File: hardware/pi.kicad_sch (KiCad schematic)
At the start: 15 parts, among them J1 PI_40PIN_STACK, J10 DISP PWR 5V, J2 PI_BREAKOUT, J3 UART0 ttyAMA0, J4 UART2 ttyAMA2, J5 UART3 ttyAMA3, J6 UART4 ttyAMA4, J7 UART5 ttyAMA5, J8 I2C1 spare, J9 FAN 5V

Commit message: feat: MPN table merged into schematic fields; SES import script
Co-Authored-By: Claude Fable 5 <noreply@anthropic.com>
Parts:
- F2: MPN (none) -> Bourns MF-R200
- J1: MPN (none) -> Adafruit 1979 (2x20 stacking, extra-tall ~19.5mm) or ESQ-12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
- J10: MPN (none) -> JST B2B-XH-A(LF)(SN)
- J3, J4, J5, J6, J7, J8: MPN (none) -> JST B4B-XH-A(LF)(SN)
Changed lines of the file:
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@@
     (property "Datasheet" "" (at 69.85 95.25 0)
+      (effects (font (size 1.27 1.27)) (hide yes)))
+    (property "MPN" "Adafruit 1979 (2x20 stacking, extra-tall ~19.5mm) or ESQ-120-39-G-D" (at 69.85 95.25 0)
       (effects (font (size 1.27 1.27)) (hide yes)))
     (pin "1")
@@
     (property "Datasheet" "" (at 229.87 69.85 0)
       (effects (font (size 1.27 1.27)) (hide yes)))
+    (property "MPN" "JST B4B-XH-A(LF)(SN)" (at 229.87 69.85 0)
+      (effects (font (size 1.27 1.27)) (hide yes)))
     (pin "1")
     (pin "2")
@@
     (property "Datasheet" "" (at 260.35 69.85 0)
       (effects (font (size 1.27 1.27)) (hide yes)))
+    (property "MPN" "JST B4B-XH-A(LF)(SN)" (at 260.35 69.85 0)
+      (effects (font (size 1.27 1.27)) (hide yes)))
     (pin "1")
     (pin "2")
@@
     (property "Datasheet" "" (at 289.56 69.85 0)
       (effects (font (size 1.27 1.27)) (hide yes)))
+    (property "MPN" "JST B4B-XH-A(LF)(SN)" (at 289.56 69.85 0)
+      (effects (font (size 1.27 1.27)) (hide yes)))
     (pin "1")
     (pin "2")
@@
     (property "Datasheet" "" (at 320.04 69.85 0)
       (effects (font (size 1.27 1.27)) (hide yes)))
+    (property "MPN" "JST B4B-XH-A(LF)(SN)" (at 320.04 69.85 0)
+      (effects (font (size 1.27 1.27)) (hide yes)))
     (pin "1")
     (pin "2")
@@
     (property "Datasheet" "" (at 350.52 69.85 0)
       (effects (font (size 1.27 1.27)) (hide yes)))
+    (property "MPN" "JST B4B-XH-A(LF)(SN)" (at 350.52 69.85 0)
+      (effects (font (size 1.27 1.27)) (hide yes)))
     (pin "1")
     (pin "2")
@@
       (effects (font (size 1.27 1.27)) (hide yes)))
     (property "Datasheet" "" (at 229.87 119.38 0)
+      (effects (font (size 1.27 1.27)) (hide yes)))
+    (property "MPN" "JST B4B-XH-A(LF)(SN)" (at 229.87 119.38 0)
       (effects (font (size 1.27 1.27)) (hide yes)))
     (pin "1")
@@
     (property "Datasheet" "" (at 350.52 119.38 0)
       (effects (font (size 1.27 1.27)) (hide yes)))
+    (property "MPN" "Bourns MF-R200" (at 350.52 119.38 0)
+      (effects (font (size 1.27 1.27)) (hide yes)))
     (pin "1")
     (pin "2")
@@
     (property "Datasheet" "" (at 379.73 119.38 0)
       (effects (font (size 1.27 1.27)) (hide yes)))
-    (pin "1")
+    (property "MPN" "JST B2B-XH-A(LF)(SN)" (at 379.73 119.38 0)
+      (effects (font (size 1.27 1.27)) (hide yes)))
+    (pin "1")

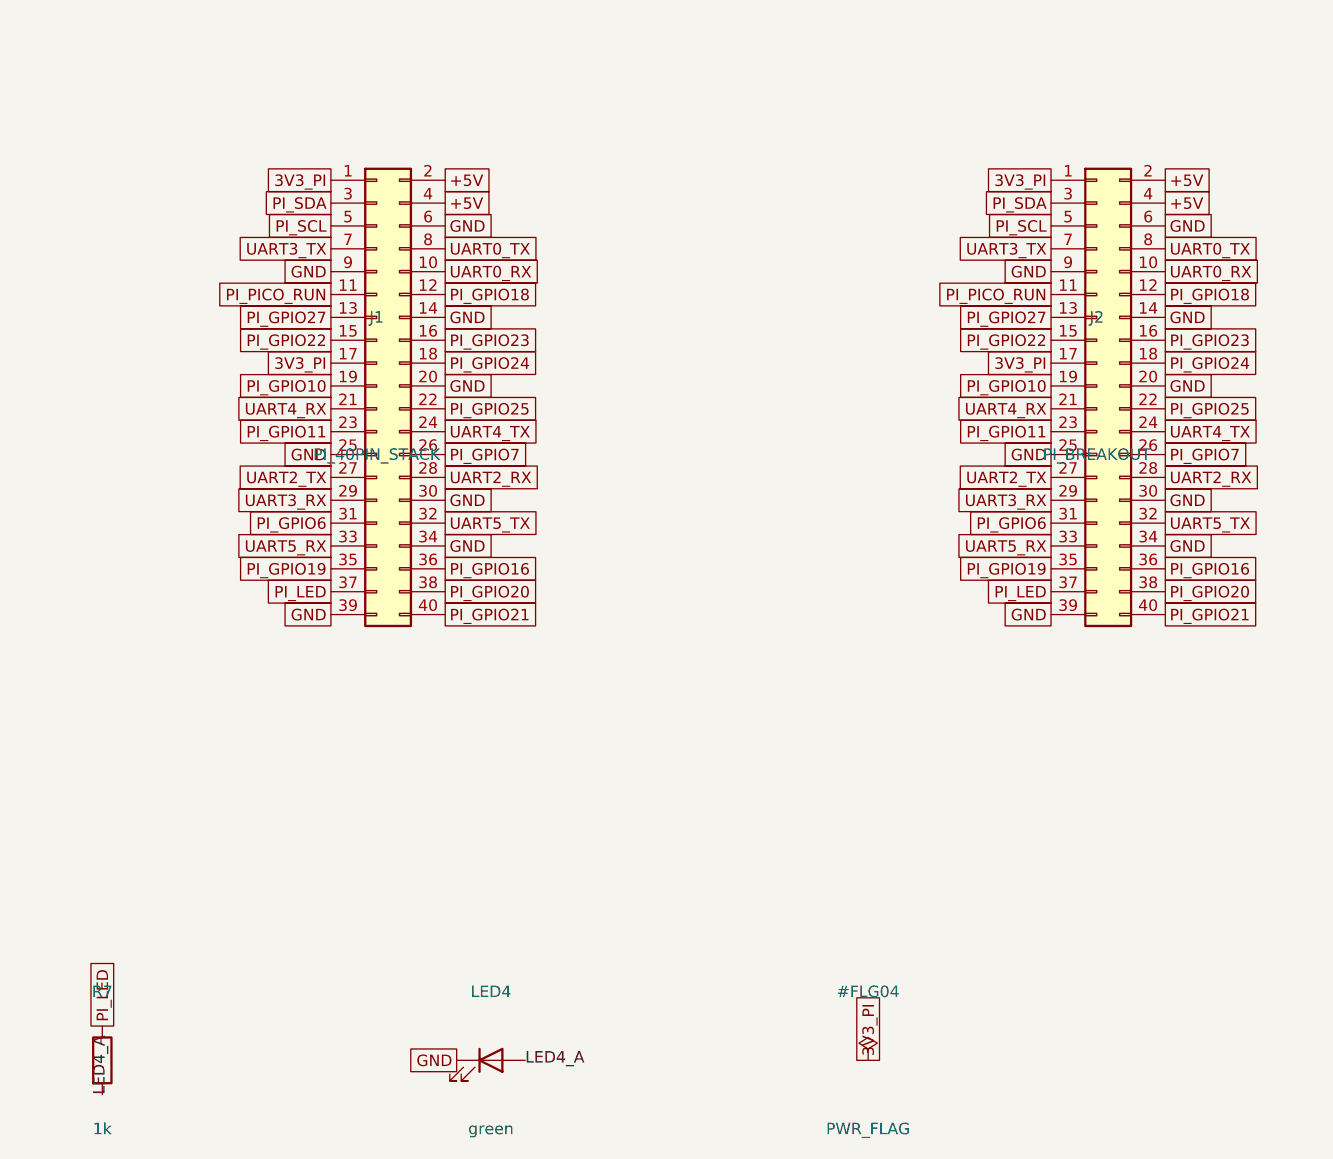
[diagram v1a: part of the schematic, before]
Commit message: cost pass 10 (schematic): remove on-board H-bridge, add J13 external-driver header (IBT-2 pinout); ERC 0, gate PASS
Co-Authored-By: Claude Fable 5 <noreply@anthropic.com>
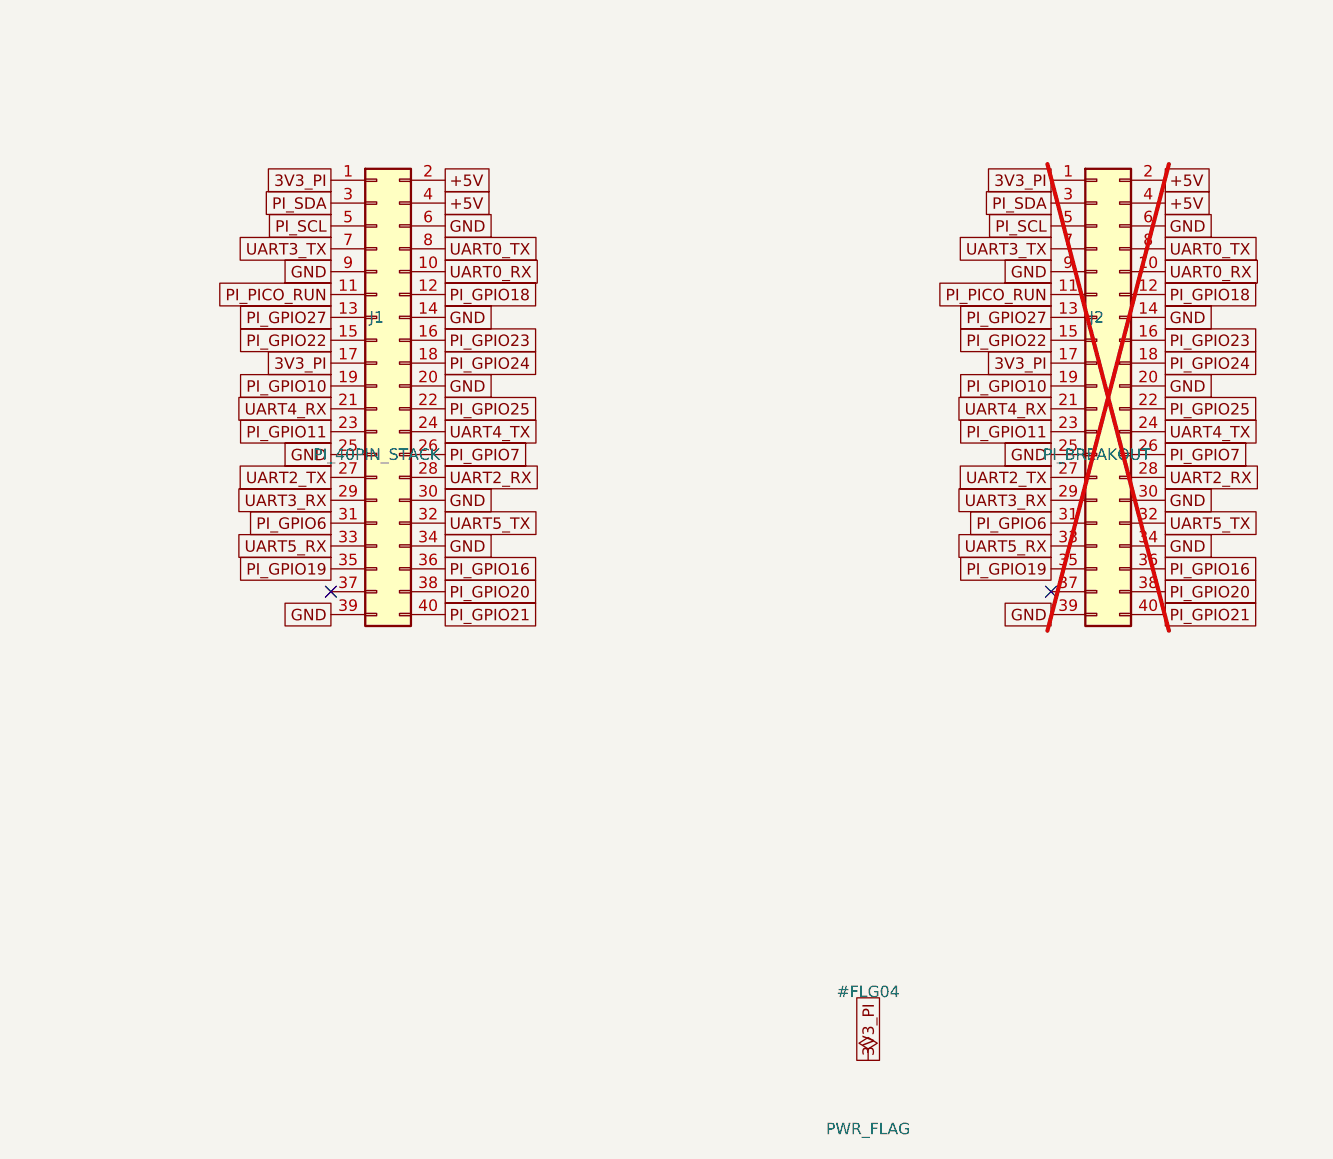
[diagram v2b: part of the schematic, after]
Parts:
- removed LED4: green, LED_THT:LED_D5.0mm, symbol Device:LED
- removed R7: 1k, Resistor_THT:R_Axial_DIN0207_L6.3mm_D2.5mm_P10.16mm_Horizontal, symbol Device:R
- J2: now not fitted
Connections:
- net PI_LED: no longer names the net of J1.37 (Pin_37)
- net PI_LED: no longer J2.37 (Pin_37)
- no-connect marks 0 -> 2
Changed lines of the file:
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@@
   )
   (symbol (lib_id "Connector_Generic:Conn_02x20_Odd_Even") (at 149.86 95.25 0) (unit 1)
-    (exclude_from_sim no) (in_bom yes) (on_board yes) (dnp no)
+    (exclude_from_sim no) (in_bom yes) (on_board yes) (dnp yes)
     (property "Reference" "J2" (at 149.86 87.63 0)
       (effects (font (size 1.27 1.27))))
@@
     (instances (project "vanchor-helm" (path "/a0000000-0000-4000-8000-000000000001/c0000000-0000-4000-8000-000000000003" (reference "J10") (unit 1))))
   )
-  (symbol (lib_id "Device:R") (at 39.37 170.18 0) (unit 1)
-    (exclude_from_sim no) (in_bom yes) (on_board yes) (dnp no)
-    (property "Reference" "R7" (at 39.37 162.56 0)
-      (effects (font (size 1.27 1.27))))
-    (property "Value" "1k" (at 39.37 177.8 0)
-      (effects (font (size 1.27 1.27))))
-    (property "Footprint" "Resistor_THT:R_Axial_DIN0207_L6.3mm_D2.5mm_P10.16mm_Horizontal" (at 39.37 170.18 0)
-      (effects (font (size 1.27 1.27)) (hide yes)))
-    (property "Datasheet" "" (at 39.37 170.18 0)
-      (effects (font (size 1.27 1.27)) (hide yes)))
-    (pin "1")
-    (pin "2")
-    (instances (project "vanchor-helm" (path "/a0000000-0000-4000-8000-000000000001/c0000000-0000-4000-8000-000000000003" (reference "R7") (unit 1))))
-  )
-  (symbol (lib_id "Device:LED") (at 82.55 170.18 0) (unit 1)
-    (exclude_from_sim no) (in_bom yes) (on_board yes) (dnp no)
-    (property "Reference" "LED4" (at 82.55 162.56 0)
-      (effects (font (size 1.27 1.27))))
-    (property "Value" "green" (at 82.55 177.8 0)
-      (effects (font (size 1.27 1.27))))
-    (property "Footprint" "LED_THT:LED_D5.0mm" (at 82.55 170.18 0)
-      (effects (font (size 1.27 1.27)) (hide yes)))
-    (property "Datasheet" "" (at 82.55 170.18 0)
-      (effects (font (size 1.27 1.27)) (hide yes)))
-    (pin "1")
-    (pin "2")
-    (instances (project "vanchor-helm" (path "/a0000000-0000-4000-8000-000000000001/c0000000-0000-4000-8000-000000000003" (reference "LED4") (unit 1))))
-  )
   (symbol (lib_id "power:PWR_FLAG") (at 124.46 170.18 0) (unit 1)
     (exclude_from_sim no) (in_bom yes) (on_board yes) (dnp no)
@@
       (effects (font (size 1.27 1.27)) (hide yes)))
   )
-  (global_label "PI_LED" (shape passive) (at 64.77 118.11 180.0) (fields_autoplaced yes)
-    (effects (font (size 1.27 1.27)) (justify right))
-    (property "Intersheetrefs" "${INTERSHEET_REFS}" (at 64.77 118.11 0)
-      (effects (font (size 1.27 1.27)) (hide yes)))
-  )
   (global_label "PI_GPIO20" (shape passive) (at 77.47 118.11 0.0) (fields_autoplaced yes)
     (effects (font (size 1.27 1.27)) (justify left))
@@
       (effects (font (size 1.27 1.27)) (hide yes)))
   )
-  (global_label "PI_LED" (shape passive) (at 144.78 118.11 180.0) (fields_autoplaced yes)
-    (effects (font (size 1.27 1.27)) (justify right))
-    (property "Intersheetrefs" "${INTERSHEET_REFS}" (at 144.78 118.11 0)
-      (effects (font (size 1.27 1.27)) (hide yes)))
-  )
   (global_label "PI_GPIO20" (shape passive) (at 157.48 118.11 0.0) (fields_autoplaced yes)
     (effects (font (size 1.27 1.27)) (justify left))
@@
       (effects (font (size 1.27 1.27)) (hide yes)))
   )
-  (global_label "PI_LED" (shape passive) (at 39.37 166.37 90.0) (fields_autoplaced yes)
-    (effects (font (size 1.27 1.27)) (justify left))
-    (property "Intersheetrefs" "${INTERSHEET_REFS}" (at 39.37 166.37 0)
-      (effects (font (size 1.27 1.27)) (hide yes)))
-  )
-  (label "LED4_A" (at 39.37 173.99 270.0) (fields_autoplaced yes)
-    (effects (font (size 1.27 1.27)) (justify left))
-  )
-  (label "LED4_A" (at 86.36 170.18 0.0) (fields_autoplaced yes)
-    (effects (font (size 1.27 1.27)) (justify left))
-  )
-  (global_label "GND" (shape passive) (at 78.74 170.18 180.0) (fields_autoplaced yes)
-    (effects (font (size 1.27 1.27)) (justify right))
-    (property "Intersheetrefs" "${INTERSHEET_REFS}" (at 78.74 170.18 0)
-      (effects (font (size 1.27 1.27)) (hide yes)))
-  )
   (global_label "3V3_PI" (shape passive) (at 124.46 170.18 270.0) (fields_autoplaced yes)
     (effects (font (size 1.27 1.27)) (justify left))
@@
       (effects (font (size 1.27 1.27)) (hide yes)))
   )
+  (no_connect (at 64.77 118.11))
+  (no_connect (at 144.78 118.11))
 )

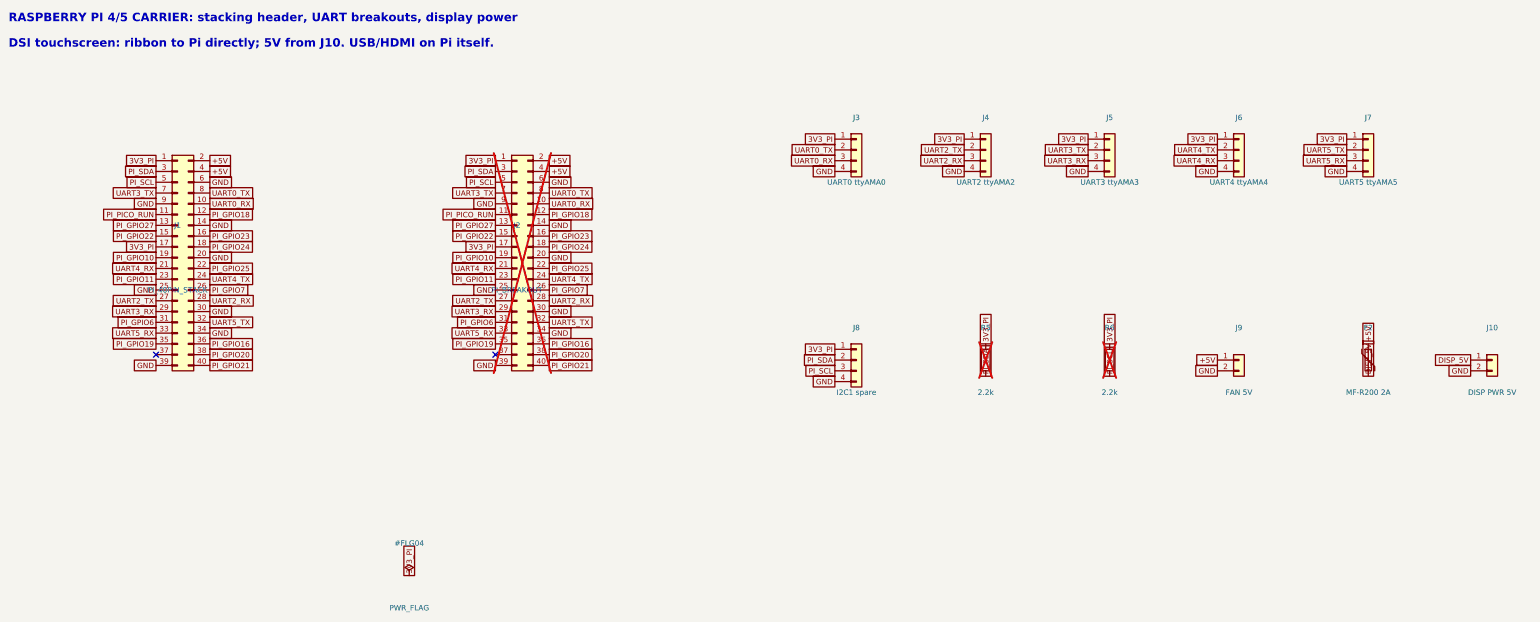
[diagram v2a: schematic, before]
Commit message: feat: v4 Orange Pi Zero 3 carrier — 125x95mm, 26-pin socket, module-on-top, DRC clean
Co-Authored-By: Claude Fable 5 <noreply@anthropic.com>
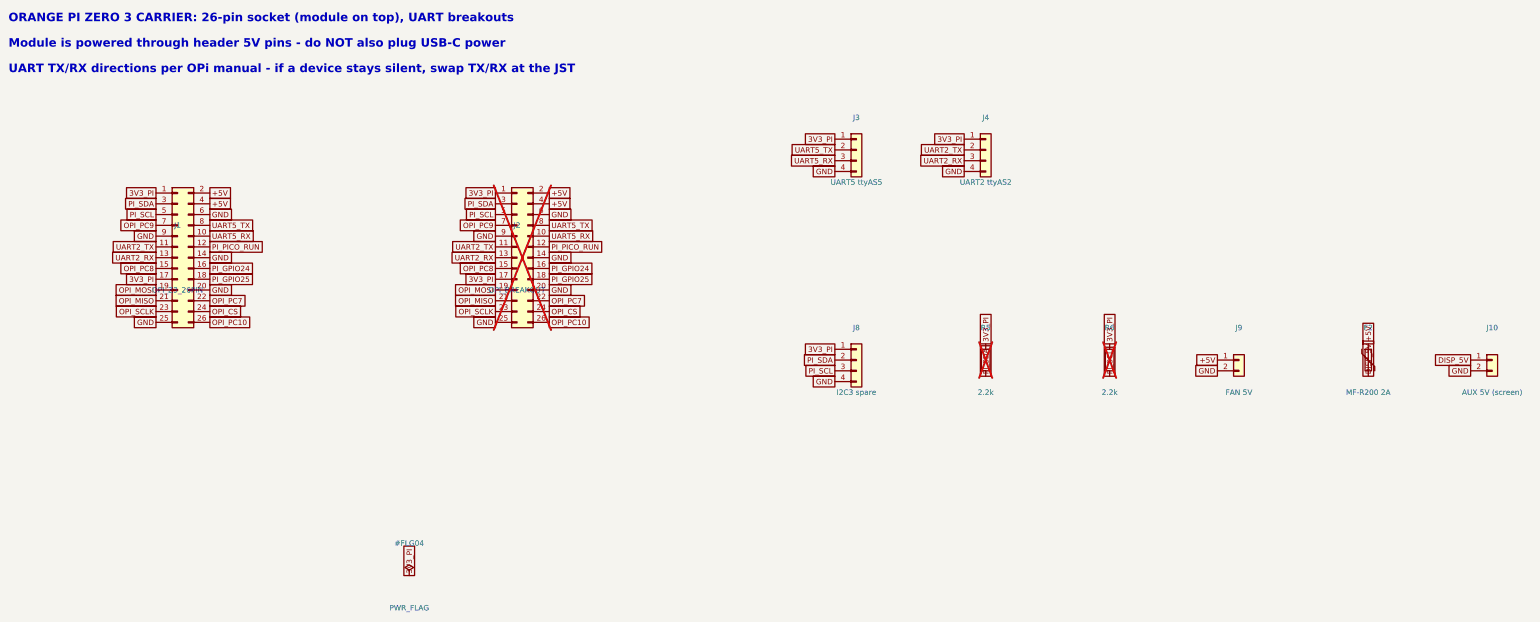
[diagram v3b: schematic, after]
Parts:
- removed J5: UART3 ttyAMA3, Connector_JST:JST_XH_B4B-XH-A_1x04_P2.50mm_Vertical, symbol Connector_Generic:Conn_01x04
- removed J6: UART4 ttyAMA4, Connector_JST:JST_XH_B4B-XH-A_1x04_P2.50mm_Vertical, symbol Connector_Generic:Conn_01x04
- removed J7: UART5 ttyAMA5, Connector_JST:JST_XH_B4B-XH-A_1x04_P2.50mm_Vertical, symbol Connector_Generic:Conn_01x04
- J1: value PI_40PIN_STACK -> OPI_Z3_26PIN; footprint Connector_PinSocket_2.54mm:PinSocket_2x20_P2.54mm_Vertical -> Connector_PinSocket_2.54mm:PinSocket_2x13_P2.54mm_Vertical; symbol Connector_Generic:Conn_02x20_Odd_Even -> Connector_Generic:Conn_02x13_Odd_Even
- J10: value DISP PWR 5V -> AUX 5V (screen)
- J2: value PI_BREAKOUT -> OPI_BREAKOUT; footprint Connector_PinHeader_2.54mm:PinHeader_2x20_P2.54mm_Vertical -> Connector_PinHeader_2.54mm:PinHeader_2x13_P2.54mm_Vertical; symbol Connector_Generic:Conn_02x20_Odd_Even -> Connector_Generic:Conn_02x13_Odd_Even
- J3: value UART0 ttyAMA0 -> UART5 ttyAS5
- J4: value UART2 ttyAMA2 -> UART2 ttyAS2
- J8: value I2C1 spare -> I2C3 spare
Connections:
- net PI_GPIO18 is gone; now on net PI_PICO_RUN: J1.12 (Pin_12), J2.12 (Pin_12)
- net PI_GPIO23 is gone; now on net PI_GPIO24: J1.16 (Pin_16), J2.16 (Pin_16)
- net PI_GPIO27 is gone; now on net UART2_RX: J1.13 (Pin_13), J2.13 (Pin_13)
- net UART0_RX is gone; now on net UART5_RX: J1.10 (Pin_10), J2.10 (Pin_10), J3.3 (Pin_3)
- net UART0_TX is gone; now on net UART5_TX: J1.8 (Pin_8), J2.8 (Pin_8), J3.2 (Pin_2)
- net GND: no longer J1.30 (Pin_30), J1.34 (Pin_34), J1.39 (Pin_39), J2.30 (Pin_30), J2.34 (Pin_34), J2.39 (Pin_39)
- net PI_GPIO24: no longer J1.18 (Pin_18), J2.18 (Pin_18)
- net PI_GPIO25: now also J1.18 (Pin_18), J2.18 (Pin_18); no longer J1.22 (Pin_22), J2.22 (Pin_22)
- net PI_PICO_RUN: no longer J1.11 (Pin_11), J2.11 (Pin_11)
- net UART2_RX: no longer J1.28 (Pin_28), J2.28 (Pin_28)
- net UART2_TX: now also J1.11 (Pin_11), J2.11 (Pin_11); no longer J1.27 (Pin_27), J2.27 (Pin_27)
- net UART5_RX: no longer J1.33 (Pin_33), J2.33 (Pin_33)
- net UART5_TX: no longer J1.32 (Pin_32), J2.32 (Pin_32)
- net PI_GPIO10 renamed OPI_MOSI
- net PI_GPIO11 renamed OPI_SCLK
- removed net PI_GPIO16: J1.36 (Pin_36), J2.36 (Pin_36)
- removed net PI_GPIO19: J1.35 (Pin_35), J2.35 (Pin_35)
- removed net PI_GPIO20: J1.38 (Pin_38), J2.38 (Pin_38)
- removed net PI_GPIO21: J1.40 (Pin_40), J2.40 (Pin_40)
- net PI_GPIO22 renamed OPI_PC8
- removed net PI_GPIO6: J1.31 (Pin_31), J2.31 (Pin_31)
- net PI_GPIO7 renamed OPI_PC10
- removed net UART3_RX: J1.29 (Pin_29), J2.29 (Pin_29)
- net UART3_TX renamed OPI_PC9
- net UART4_RX renamed OPI_MISO
- net UART4_TX renamed OPI_CS
- new net OPI_PC7: J1.22 (Pin_22), J2.22 (Pin_22)
- no-connect marks 2 -> 0
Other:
- note added: "Module is powered through header 5V pins - do NOT also plug USB-C power"
- note added: "ORANGE PI ZERO 3 CARRIER: 26-pin socket (module on top), UART breakouts"
- note added: "UART TX/RX directions per OPi manual - if a device stays silent, swap TX/RX at the JST"
- note removed: "DSI touchscreen: ribbon to Pi directly; 5V from J10. USB/HDMI on Pi itself."
- note removed: "RASPBERRY PI 4/5 CARRIER: stacking header, UART breakouts, display power"
